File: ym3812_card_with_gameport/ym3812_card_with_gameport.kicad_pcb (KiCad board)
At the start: 2 copper layers, 115.6 x 106.7 mm, 79 parts, among them IC1 74LS138, IC11 NE558, IC12 74HCT02, IC13 74LS74, IC18 74LS244, IC2 74LS138, IC3 74LS138, IC4 74LS245, IC6 YM3812, IC7 Y3014B, IC8 LM324, IC9 TDA7233, J1 Bus_ISA_8bit

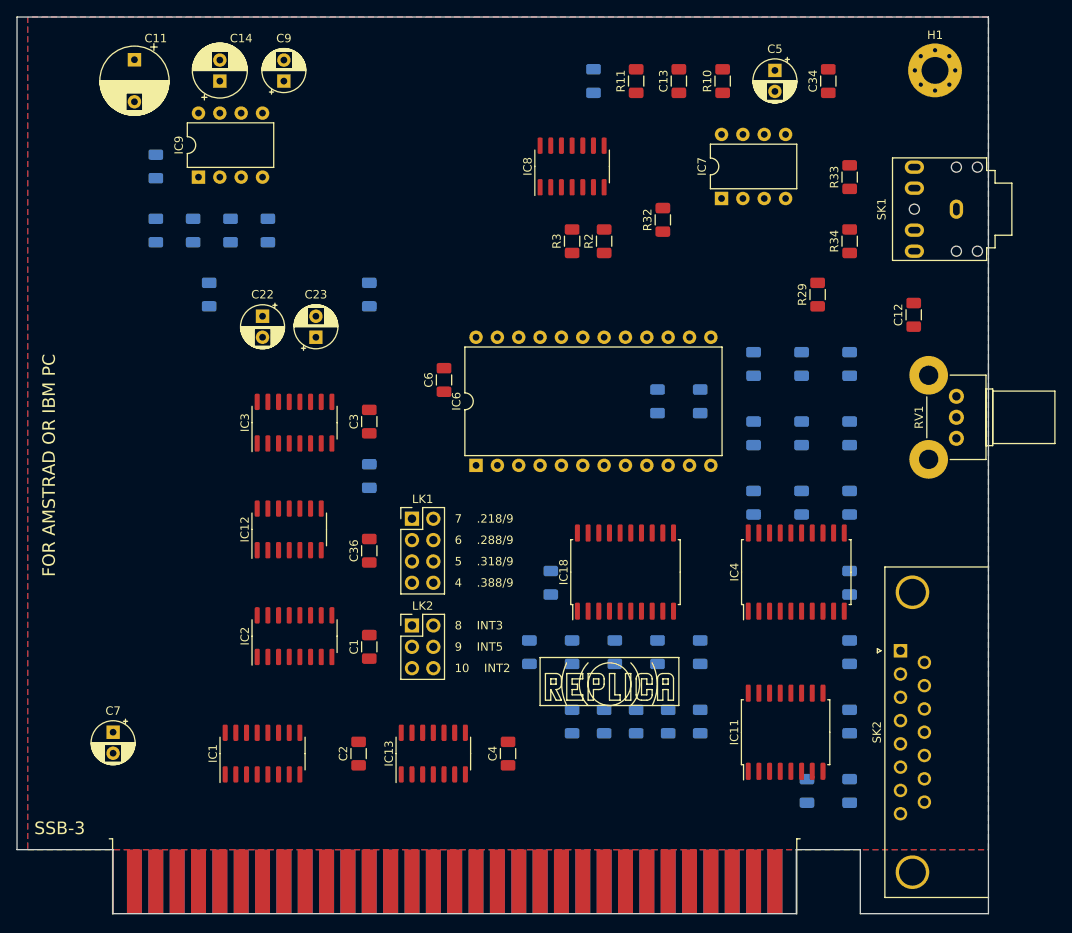
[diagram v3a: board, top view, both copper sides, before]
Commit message: corrections and some new traces
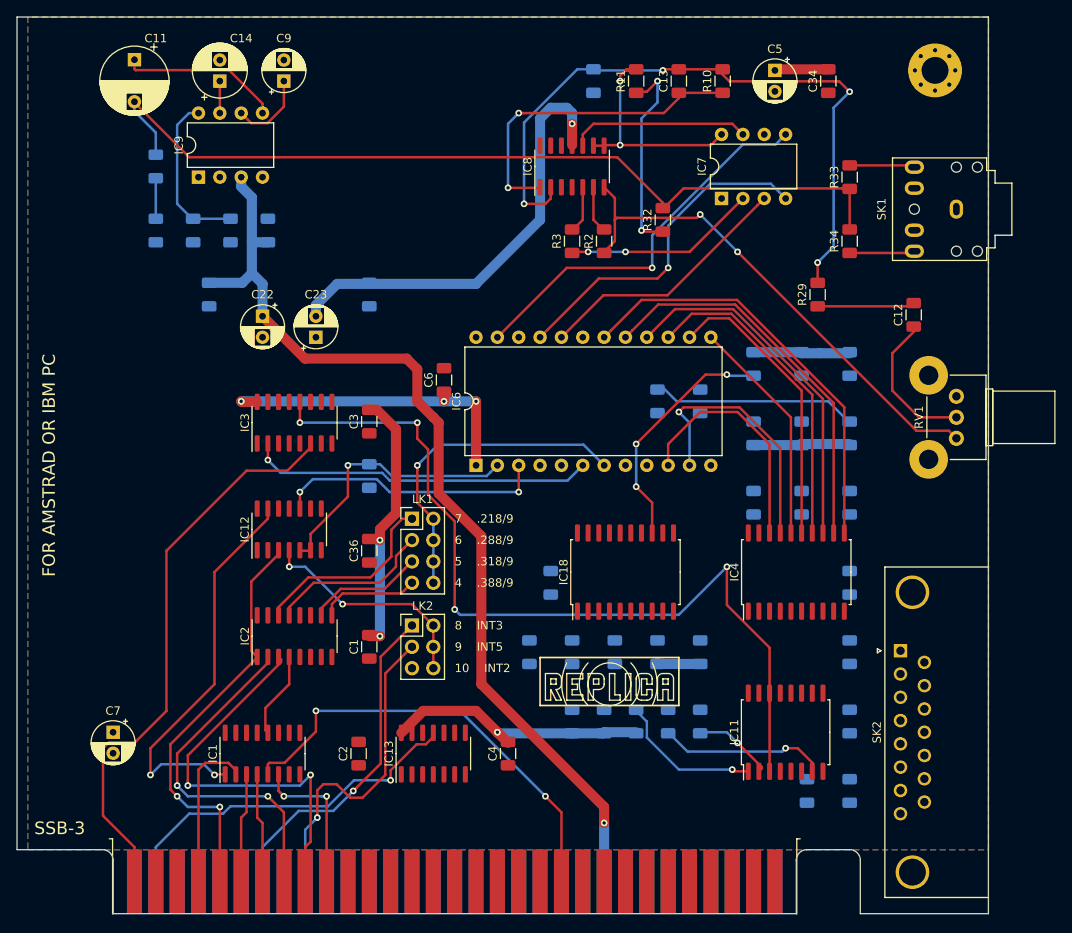
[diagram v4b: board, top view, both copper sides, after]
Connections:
- C13 pad 1: Net-(C13-Pad1) -> /PREAMP_OUT
- C13 pad 2: +5V -> Net-(C13-Pad2)
- IC8 pad 2: Net-(C13-Pad1) -> Net-(C13-Pad2)
- R10 pad 1: Net-(C13-Pad1) -> /PREAMP_OUT
- R10 pad 2: +5V -> Net-(C13-Pad2)
- R11 pad 1: /DAC_MP -> GND
- R11 pad 2: GND -> /DAC_MP
- R29 pad 2: Net-(C13-Pad1) -> Net-(C13-Pad2)
- R9 pad 2: /PREAMP_OUT -> Net-(C13-Pad2)
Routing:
- net +5V: track 0.00 -> 135.9 mm, vias 0 -> 6
- net +12V: track 0.00 -> 116.3 mm, vias 0 -> 1
- net /AUDIO_OUT: track 0.00 -> 104.1 mm
- net /JOY_TR: track 0.00 -> 101.8 mm, vias 0 -> 4
- net Net-(C13-Pad2): track 0.00 -> 81.8 mm, vias 0 -> 4
- net /BA00: track 0.00 -> 68.5 mm
- net Net-(IC8-Pad7): track 0.00 -> 60.7 mm, vias 0 -> 2
- net /AEN: track 0.00 -> 53.5 mm, vias 0 -> 2
- net -12V: track 0.00 -> 52.7 mm, vias 0 -> 1
- net /OPL_D7: track 0.00 -> 50.7 mm
- net /BA04: track 0.00 -> 49.9 mm, vias 0 -> 2
- net /BA08: track 0.00 -> 48.1 mm, vias 0 -> 2
- net /BA01_NOR_BA02: track 0.00 -> 47.5 mm, vias 0 -> 2
- net /OPL_D6: track 0.00 -> 46.7 mm
- net /OPL_SY: track 0.00 -> 46.6 mm, vias 0 -> 1
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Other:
- outline, holes or cut-outs redrawn

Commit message: minor corrections, routing complete
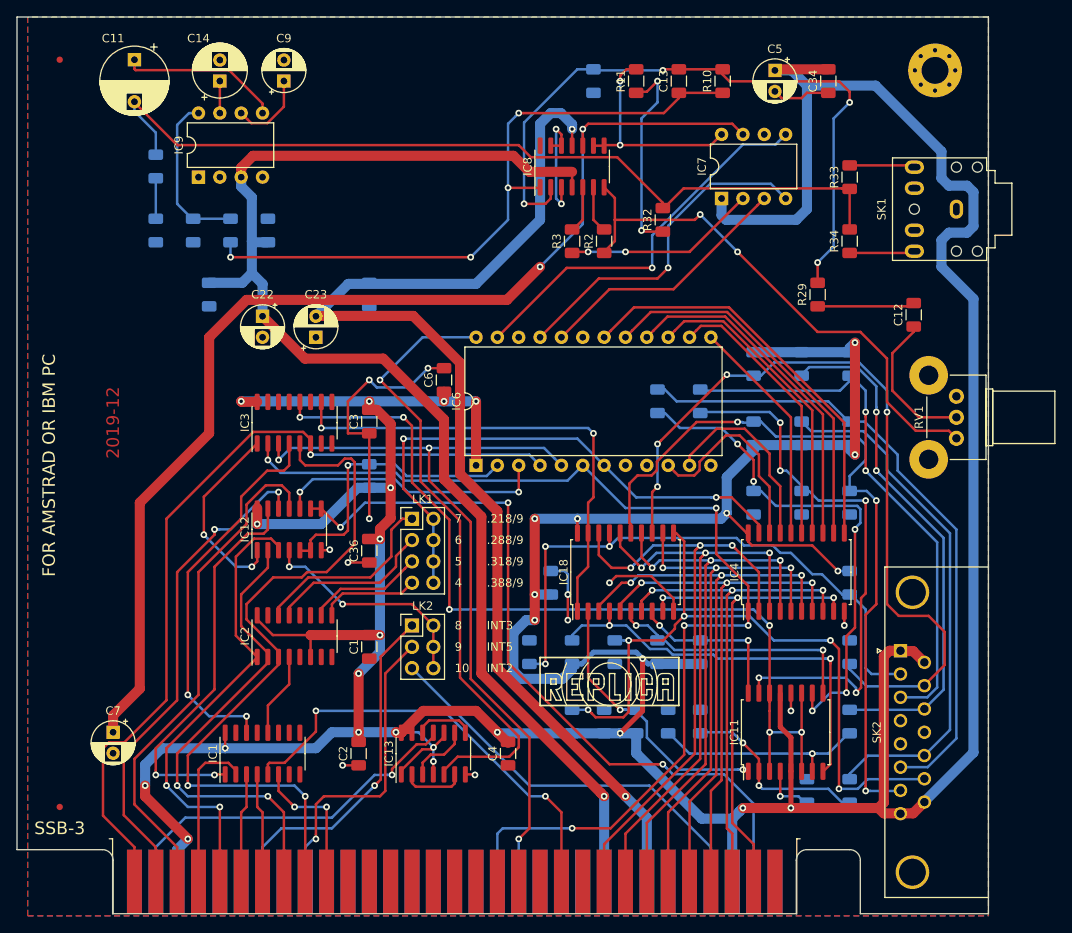
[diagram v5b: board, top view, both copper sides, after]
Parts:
- added REF**: Fiducial_0.75mm_Mask1.5mm, Fiducial:Fiducial_0.75mm_Mask1.5mm, F.Cu at (130.8, 127.0)
- added REF**: Fiducial_0.75mm_Mask1.5mm, Fiducial:Fiducial_0.75mm_Mask1.5mm, F.Cu at (130.8, 38.1)
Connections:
- C7 pad 1: +5V -> /DAC_REF
- IC2 pad 6: /BA01_NOR_BA02 -> +5V
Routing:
- net +5V: track 135.9 -> 600.6 mm, vias 6 -> 29
- net /DAC_REF: track 21.4 -> 134.8 mm, vias 0 -> 2
- net /IOW: track 0.00 -> 94.1 mm, vias 0 -> 3
- net /RESET: track 0.00 -> 90.1 mm, vias 0 -> 3
- net /IOR: track 41.1 -> 129.5 mm, vias 1 -> 5
- net /BTN2: track 0.00 -> 88.0 mm, vias 0 -> 3
- net -12V: track 52.7 -> 140.6 mm, vias 1 -> 2
- net /BTN4: track 0.00 -> 83.5 mm, vias 0 -> 5
- net GND: track 24.2 -> 104.8 mm, vias 2 -> 16
- net /OPL_CLK: track 0.00 -> 74.7 mm, vias 0 -> 1
- net /DB0: track 0.00 -> 74.2 mm, vias 0 -> 3
- net /DB1: track 0.00 -> 71.3 mm, vias 0 -> 3
- net /BTN1: track 0.00 -> 71.0 mm, vias 0 -> 3
- net /DB4: track 0.00 -> 68.7 mm, vias 0 -> 3
- net /DB2: track 0.00 -> 67.8 mm, vias 0 -> 3
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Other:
- board text added: ".218/9"
- board text added: ".288/9"
- board text added: ".318/9"
- board text added: ".388/9"
- board text added: "10"
- board text added: "2019-12"
- board text added: "4"
- board text added: "5"
- board text added: "6"
- board text added: "7"
- board text added: "8"
- board text added: "9"
- board text added: "INT2"
- board text added: "INT3"
- board text added: "INT5"
- board text removed: "10 INT2"
- board text removed: "4 .388/9"
- board text removed: "5 .318/9"
- board text removed: "6 .288/9"
- board text removed: "7 .218/9"
- board text removed: "8 INT3"
- board text removed: "9 INT5"

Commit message: layout beautification
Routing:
- net GND: track 104.8 -> 115.7 mm, vias 16 -> 20
- net +5V: track 600.6 -> 604.6 mm
- net Net-(IC8-Pad7): track 63.7 -> 60.2 mm
- net /AUDIO_OUT: track 104.1 -> 106.7 mm
- net /BA04: track 55.9 -> 57.4 mm
- net /OPL_D7: track 48.9 -> 50.2 mm
- net /BA02: track 60.8 -> 62.1 mm
- net /BA08: track 87.1 -> 88.3 mm
- net /BTN2: track 88.0 -> 86.9 mm
- net /BA07: track 57.4 -> 58.4 mm
- net /OPL_D6: track 44.9 -> 45.8 mm
- net /IOW: track 94.1 -> 93.2 mm
- net /BA03: track 19.0 -> 19.8 mm
- net /TIMING_D: track 65.5 -> 66.2 mm
- net /OPL_D2: track 27.2 -> 28.0 mm
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
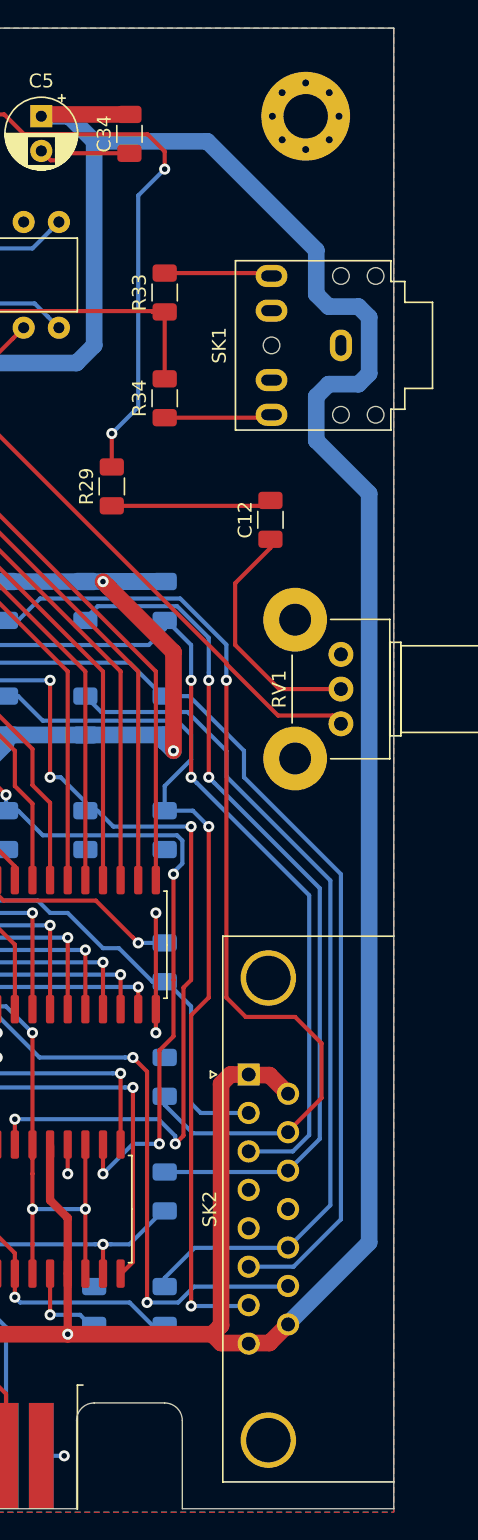
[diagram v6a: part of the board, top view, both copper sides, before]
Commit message: adapt to Keystone bracket 9200-3
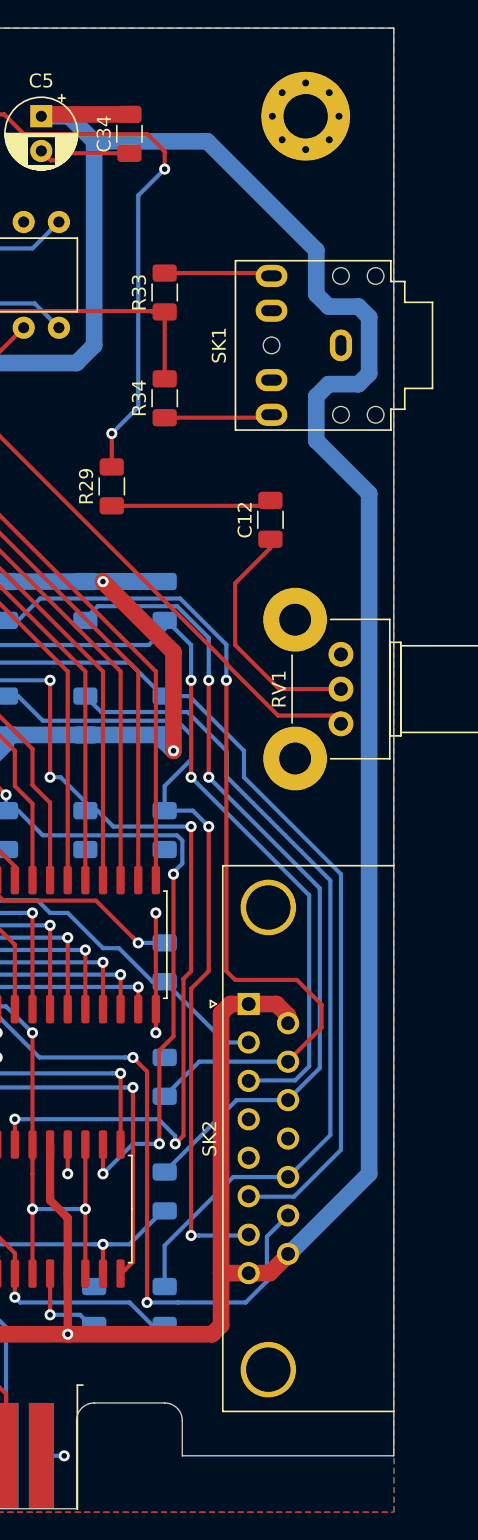
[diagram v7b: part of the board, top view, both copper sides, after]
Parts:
- moved SK2 5.08 mm to (230.8, 103.3)
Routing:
- net /BTN1: track 71.0 -> 64.8 mm
- net /BTN2: track 86.9 -> 81.8 mm
- net /JOY1: track 65.3 -> 60.2 mm
- net /JOY2: track 76.6 -> 71.5 mm
- net /BTN3: track 95.0 -> 90.0 mm
- net /BTN4: track 83.2 -> 87.3 mm
- net /JOY3: track 61.9 -> 58.8 mm
- net /JOY4: track 62.5 -> 60.8 mm
- net +5V: track 604.6 -> 604.0 mm
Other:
- outline, holes or cut-outs redrawn

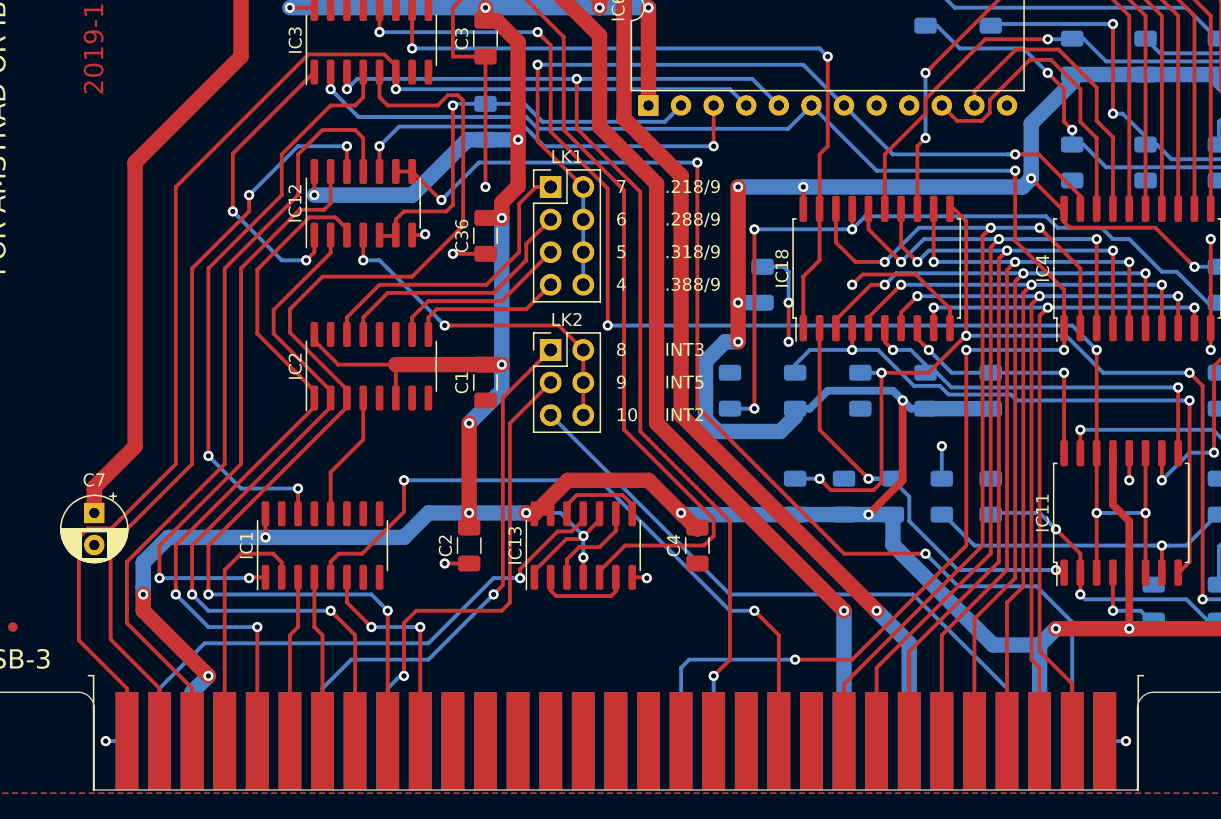
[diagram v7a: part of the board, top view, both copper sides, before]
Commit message: adjust edge connector
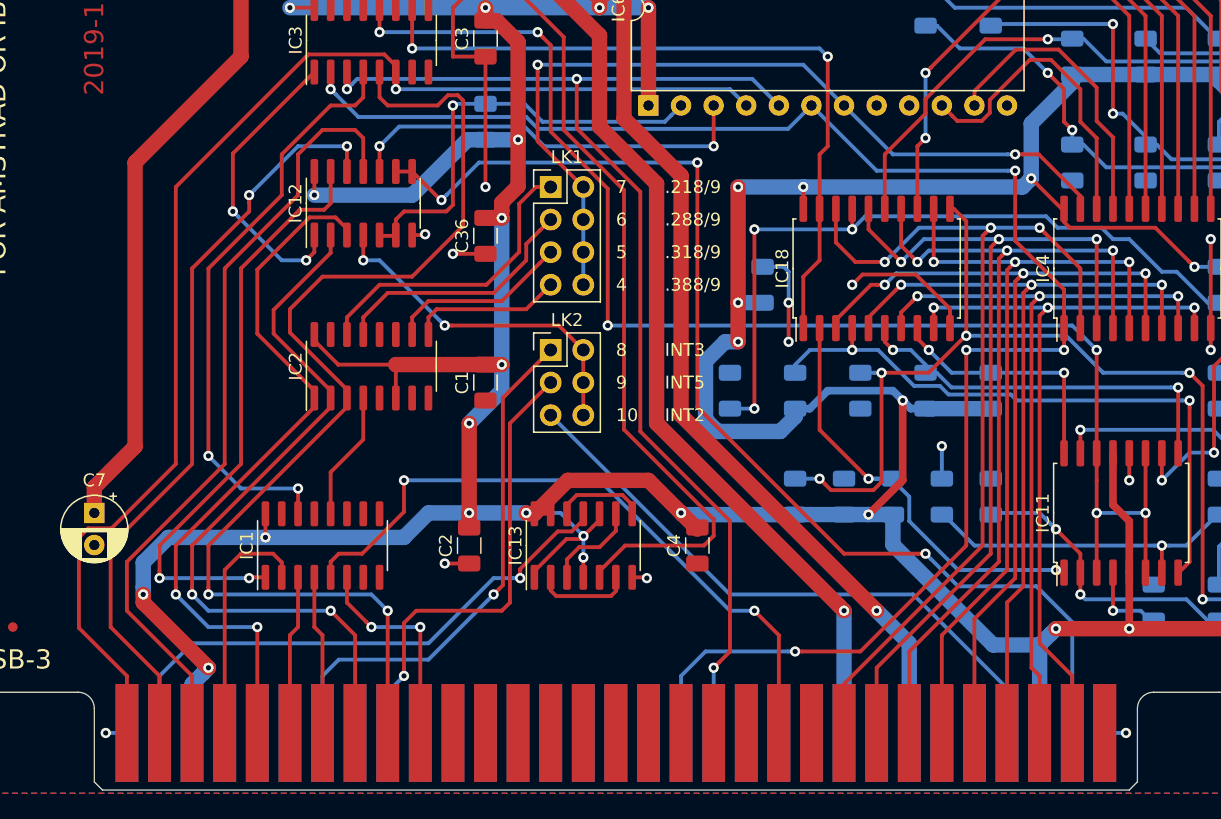
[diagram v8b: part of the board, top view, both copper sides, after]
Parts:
- moved J1 0.63 mm to (215.9, 135.3)
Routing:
- net /OSC: track 43.5 -> 44.1 mm
- net /IRQ3: track 41.4 -> 41.9 mm
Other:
- outline, holes or cut-outs redrawn
